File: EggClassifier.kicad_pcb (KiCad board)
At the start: 2 copper layers, 100 x 100 mm, 54 parts, among them J1 Left_02x24, J10 LCD_CHAR, J11 SERVO2, J12 BME280, J13 UART1, J14 FAN, J15 UART2, J16 AS7265X, J17 TFT_SPI, J2 Right Header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

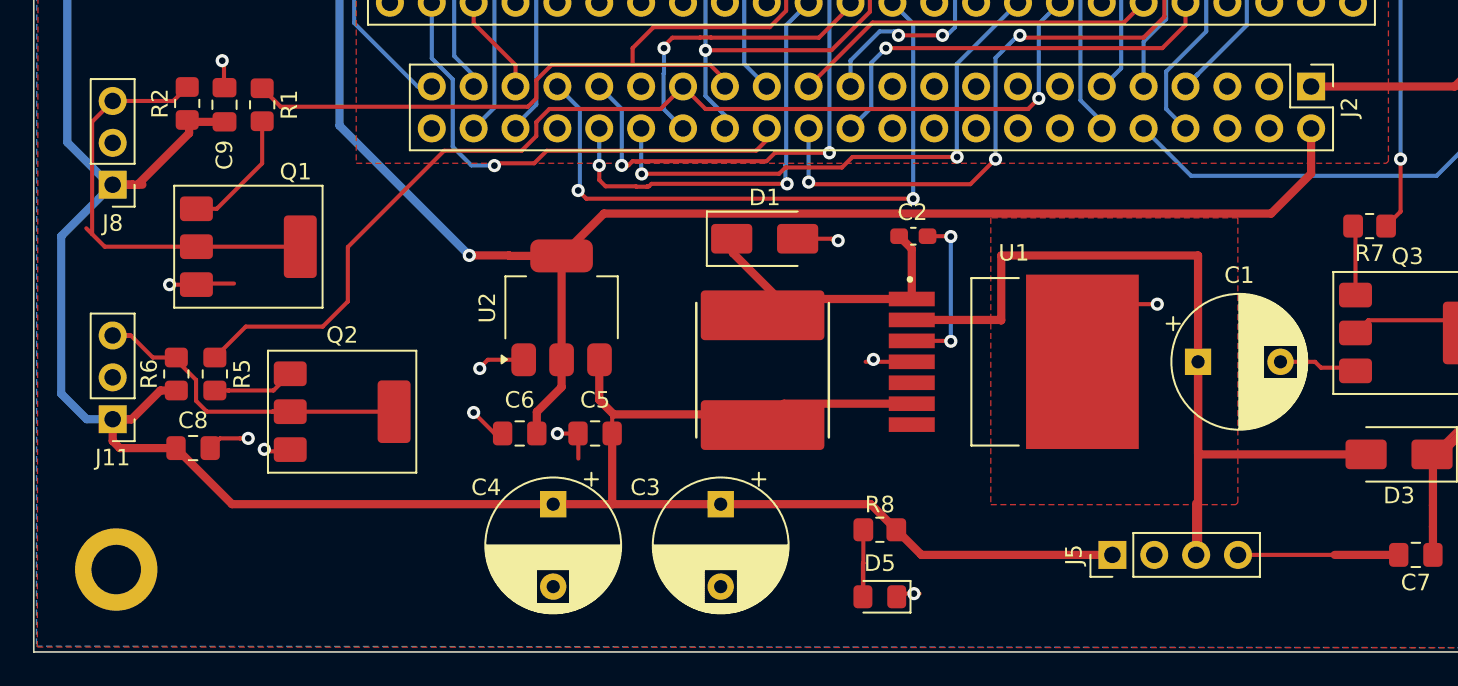
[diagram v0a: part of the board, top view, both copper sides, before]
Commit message: resize electrolytic capacitors hole size to be the same as the connector pins.
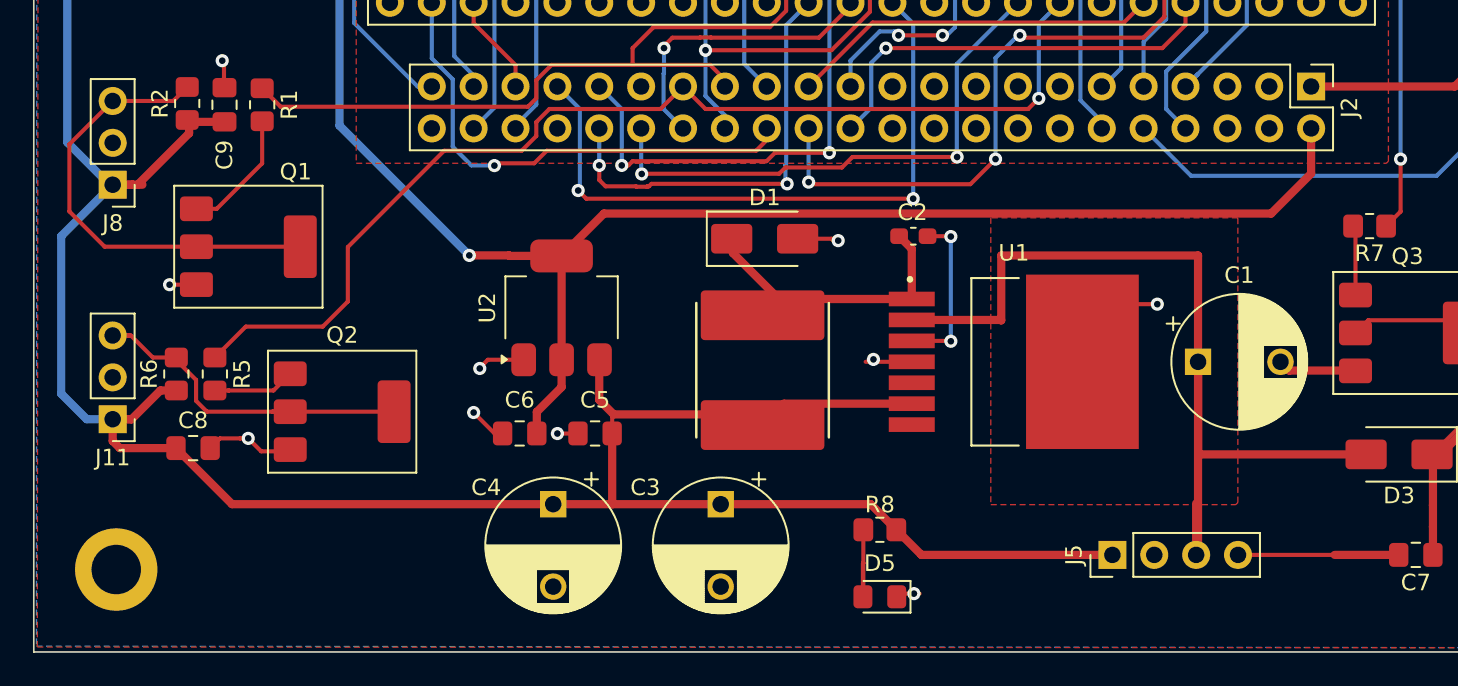
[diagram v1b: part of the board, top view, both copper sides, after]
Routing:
- net GND: track 104.3 -> 102.0 mm, vias 25 -> 24
- net Net-(J8-Pin_3): track 26.9 -> 27.6 mm
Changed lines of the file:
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@@
 		(tags "CP Radial series Radial pin pitch 5.00mm  diameter 8mm Electrolytic Capacitor")
 		(property "Reference" "C4"
-			(at -1.016 4.064 180)
+			(at -1.016 4.064 0)
 			(layer "F.SilkS")
 			(effects
@@
 		)
 		(property "Value" "100uF"
-			(at 7.902 0.508 180)
+			(at 7.902 0.508 0)
 			(layer "F.Fab")
 			(effects
@@
 			(at 0 0 270)
 			(size 1.6 1.6)
-			(drill 0.8)
+			(drill 1)
 			(layers "*.Cu" "*.Mask")
 			(remove_unused_layers no)
@@
 			(at 5 0 270)
 			(size 1.6 1.6)
-			(drill 0.8)
+			(drill 1)
 			(layers "*.Cu" "*.Mask")
 			(remove_unused_layers no)
@@
 		(tags "CP Radial series Radial pin pitch 5.00mm  diameter 8mm Electrolytic Capacitor")
 		(property "Reference" "C3"
-			(at -1.016 4.572 180)
+			(at -1.016 4.572 0)
 			(layer "F.SilkS")
 			(effects
@@
 		)
 		(property "Value" "100uF"
-			(at 7.648 0 180)
+			(at 7.648 0 0)
 			(layer "F.Fab")
 			(effects
@@
 			(at 0 0 270)
 			(size 1.6 1.6)
-			(drill 0.8)
+			(drill 1)
 			(layers "*.Cu" "*.Mask")
 			(remove_unused_layers no)
@@
 			(at 5 0 270)
 			(size 1.6 1.6)
-			(drill 0.8)
+			(drill 1)
 			(layers "*.Cu" "*.Mask")
 			(remove_unused_layers no)
@@
 			(at 0 0)
 			(size 1.6 1.6)
-			(drill 0.8)
+			(drill 1)
 			(layers "*.Cu" "*.Mask")
 			(remove_unused_layers no)
@@
 			(at 5 0)
 			(size 1.6 1.6)
-			(drill 0.8)
+			(drill 1)
 			(layers "*.Cu" "*.Mask")
 			(remove_unused_layers no)
@@
 	)
 	(segment
-		(start 107.061 122.757)
-		(end 107.542 122.276)
-		(width 0.25)
+		(start 155.622 122.4)
+		(end 156.153 122.931)
+		(width 0.5)
 		(layer "F.Cu")
 		(net 1)
 	)
 	(segment
-		(start 158.075 122.757)
-		(end 159.979 122.757)
+		(start 107.061 122.757)
+		(end 107.542 122.276)
 		(width 0.25)
 		(layer "F.Cu")
@@
 	)
 	(segment
-		(start 113.03 128.27)
-		(end 113.03 126.7675)
-		(width 0.25)
-		(layer "F.Cu")
-		(net 1)
-	)
-	(segment
-		(start 157.718 122.4)
-		(end 158.075 122.757)
-		(width 0.25)
-		(layer "F.Cu")
-		(net 1)
-	)
-	(segment
 		(start 88.2359 117.7226)
 		(end 89.8598 117.7226)
@@
 	)
 	(segment
-		(start 93.9806 127.7083)
-		(end 93.9806 127.83)
-		(width 0.25)
-		(layer "F.Cu")
-		(net 1)
-	)
-	(segment
 		(start 128.5116 115.0496)
 		(end 128.397 114.935)
@@
 	)
 	(segment
+		(start 156.153 122.931)
+		(end 160.153 122.931)
+		(width 0.5)
+		(layer "F.Cu")
+		(net 1)
+	)
+	(segment
 		(start 107.178 83.307)
 		(end 100.193 83.307)
@@
 	)
 	(segment
-		(start 155.622 122.4)
-		(end 157.718 122.4)
+		(start 93.7935 127.83)
+		(end 93.0076 127.0441)
 		(width 0.25)
 		(layer "F.Cu")
@@
 	)
 	(segment
-		(start 92.1439 117.652)
-		(end 89.9304 117.652)
-		(width 0.25)
-		(layer "F.Cu")
-		(net 1)
-	)
-	(segment
-		(start 93.9806 127.83)
-		(end 95.4496 127.83)
-		(width 0.25)
-		(layer "F.Cu")
-		(net 1)
-	)
-	(segment
 		(start 158.905 134.112)
 		(end 153.045 134.112)
@@
 		(net 1)
 	)
+	(segment
+		(start 95.4496 127.83)
+		(end 93.7935 127.83)
+		(width 0.25)
+		(layer "F.Cu")
+		(net 1)
+	)
 	(via
 		(at 88.2359 117.7226)
@@
 	)
 	(via
-		(at 93.9806 127.7083)
-		(size 0.8)
-		(drill 0.4)
-		(layers "F.Cu" "B.Cu")
-		(net 1)
-	)
-	(via
 		(at 169.0604 67.7789)
 		(size 0.8)
@@
 	)
 	(segment
-		(start 83.5376 114.6526)
-		(end 83.5376 107.8364)
+		(start 84.2976 115.4176)
+		(end 82.159 113.279)
+		(width 0.25)
+		(layer "F.Cu")
+		(net 132)
+	)
+	(segment
+		(start 82.159 113.279)
+		(end 82.159 109.2046)
 		(width 0.25)
 		(layer "F.Cu")
@@
 	)
 	(segment
-		(start 84.303 115.418)
-		(end 83.185 114.3)
+		(start 89.8648 115.4176)
+		(end 84.2976 115.4176)
 		(width 0.25)
 		(layer "F.Cu")
@@
 	)
 	(segment
-		(start 83.5376 107.8364)
-		(end 84.7852 106.5888)
+		(start 82.159 109.2046)
+		(end 84.7852 106.5784)
 		(width 0.25)
 		(layer "F.Cu")
@@
 	)
 	(segment
-		(start 96.1648 115.418)
-		(end 84.303 115.418)
+		(start 89.8648 115.4176)
+		(end 96.1648 115.4176)
 		(width 0.25)
 		(layer "F.Cu")

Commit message: snapshot
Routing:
- net USER_GPIO4: track 142.7 -> 109.8 mm
- net UART2_RX: track 58.3 -> 59.9 mm
- net +3.3V: track 250.8 -> 251.8 mm, vias 11 -> 12
- net USER_GPIO3: track 83.1 -> 83.9 mm
- net I2C1_SCL: track 71.7 -> 72.4 mm
- net UART1_RX: track 40.3 -> 39.6 mm
- net CAM_HS: track 93.2 -> 93.7 mm
- net TFT_RS: track 79.3 -> 79.2 mm, vias 5 -> 4

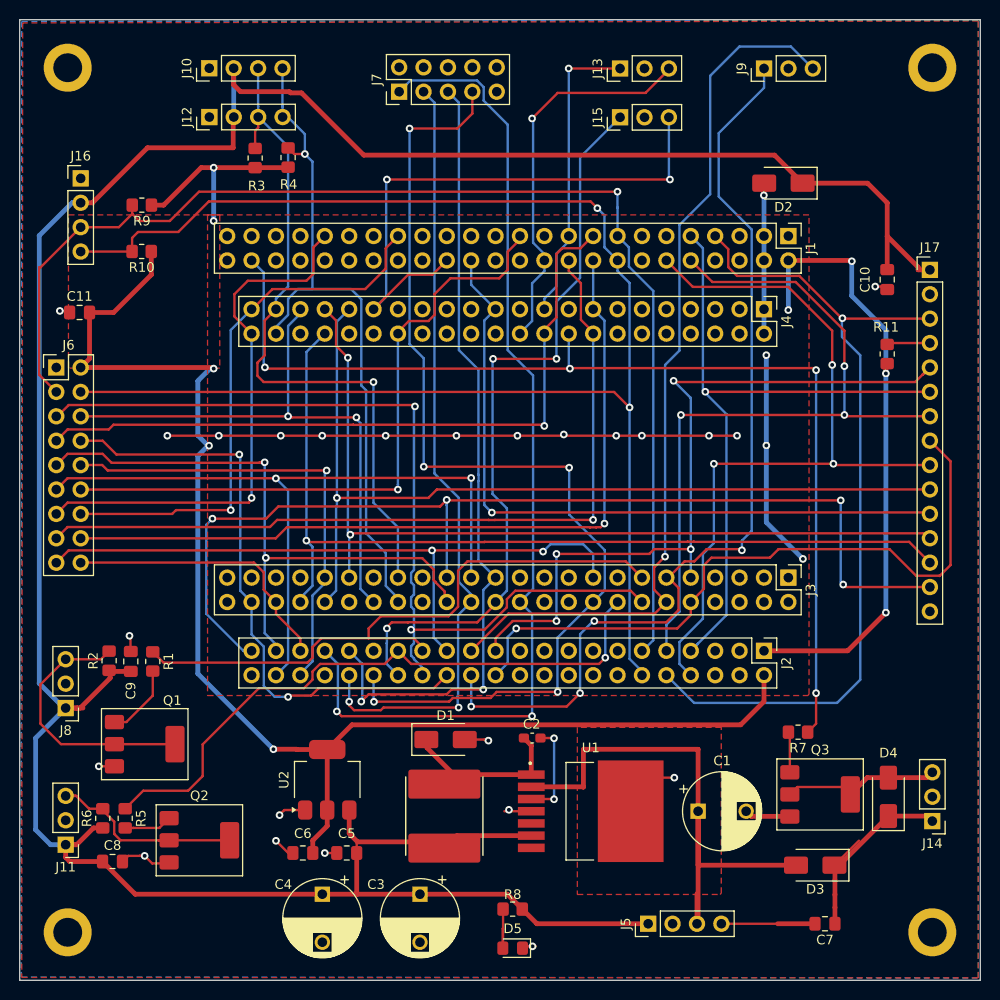
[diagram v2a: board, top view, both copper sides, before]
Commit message: change capacitor footprint
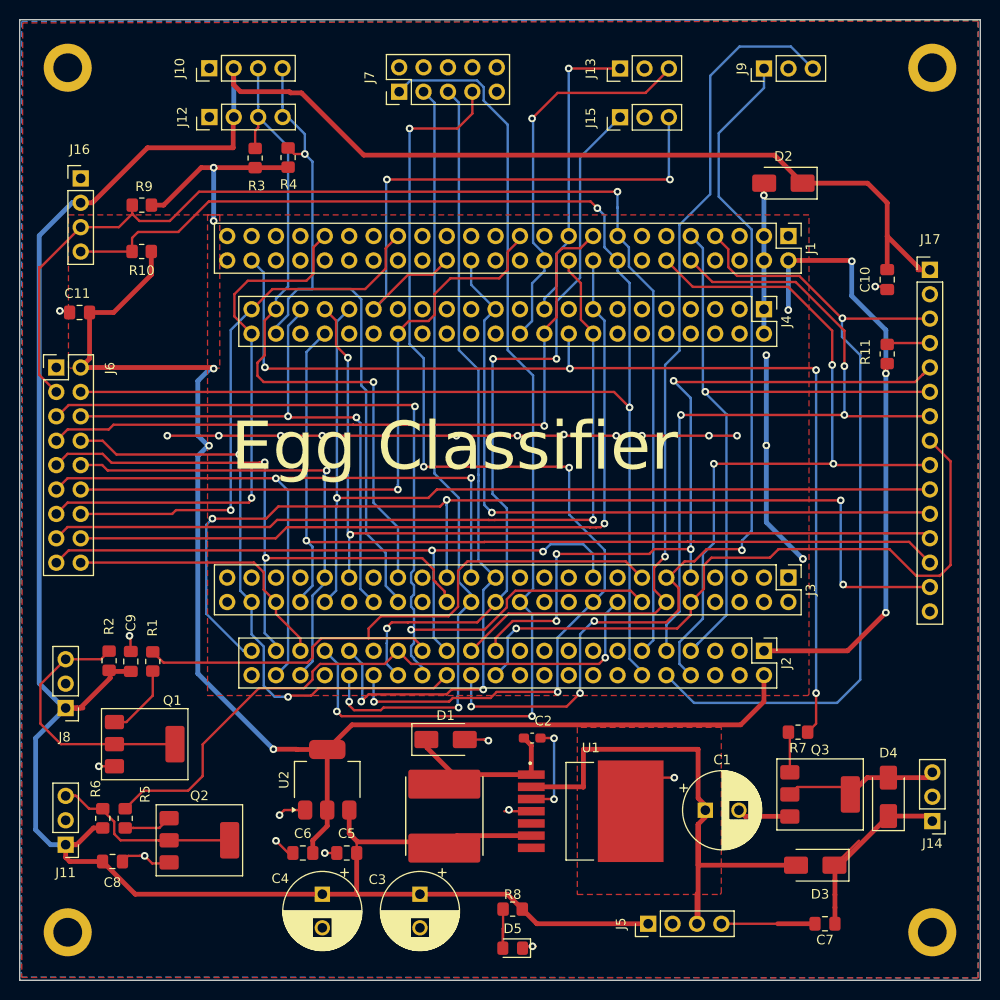
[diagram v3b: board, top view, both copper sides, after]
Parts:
- C1: footprint Capacitor_THT:CP_Radial_D8.0mm_P5.00mm -> EggClassifier:CP_Radial_D8.0mm_P3.50mm
- C3, C4: value 100uF -> 220uF; footprint Capacitor_THT:CP_Radial_D8.0mm_P5.00mm -> EggClassifier:CP_Radial_D8.0mm_P3.50mm
- moved C1 0.76 mm to (151.4, 122.3)
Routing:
- net +12V: track 58.0 -> 56.8 mm
- net GND: track 102.0 -> 102.8 mm
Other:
- board text added: "Egg Classifier"

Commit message: adjust schematic and PCB to reflect as build condition
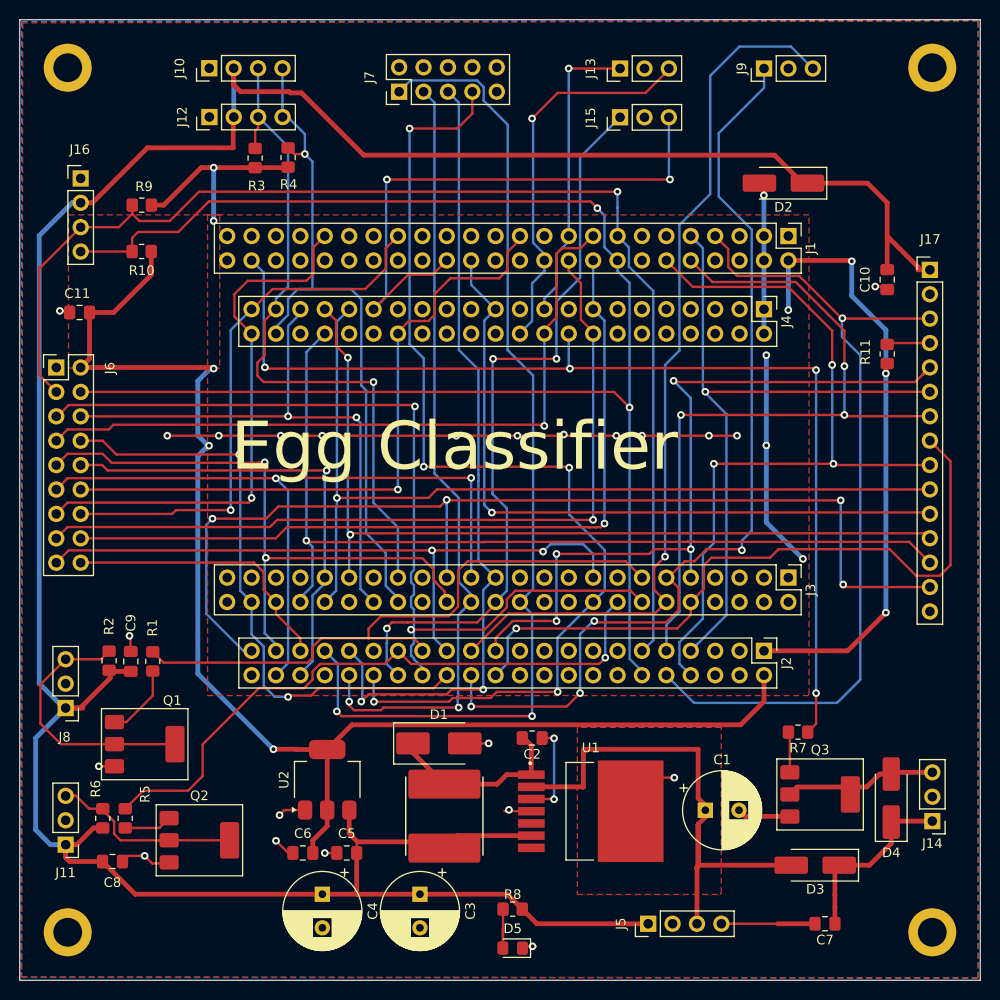
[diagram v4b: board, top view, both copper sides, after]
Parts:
- C1, C3, C4: footprint EggClassifier:CP_Radial_D8.0mm_P3.50mm -> Capacitor_THT:CP_Radial_D8.0mm_P3.50mm
- C2: value 102 -> 103; footprint Capacitor_SMD:C_0603_1608Metric_Pad1.08x0.95mm_HandSolder -> Capacitor_SMD:C_0805_2012Metric_Pad1.18x1.45mm_HandSolder
- D1: value SS36 -> SS56BF; footprint Diode_SMD:D_SMA -> Diode_SMD:D_SMB_Handsoldering
- D2, D3, D4: footprint Diode_SMD:D_SMA -> Diode_SMD:D_SMA_Handsoldering
- R11: value 10K -> 4.7K
- R8: value 330 -> 4.7K
- moved D1 0.80 mm to (123.6, 115.3)
- moved D4 0.32 mm to (170.7, 121.0)
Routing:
- net +12V: track 56.8 -> 54.1 mm
- net Net-(D1-K): track 16.9 -> 19.2 mm
- net Net-(D3-K): track 26.5 -> 24.4 mm
- net Net-(D4-A): track 16.9 -> 15.5 mm

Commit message: moved connectors
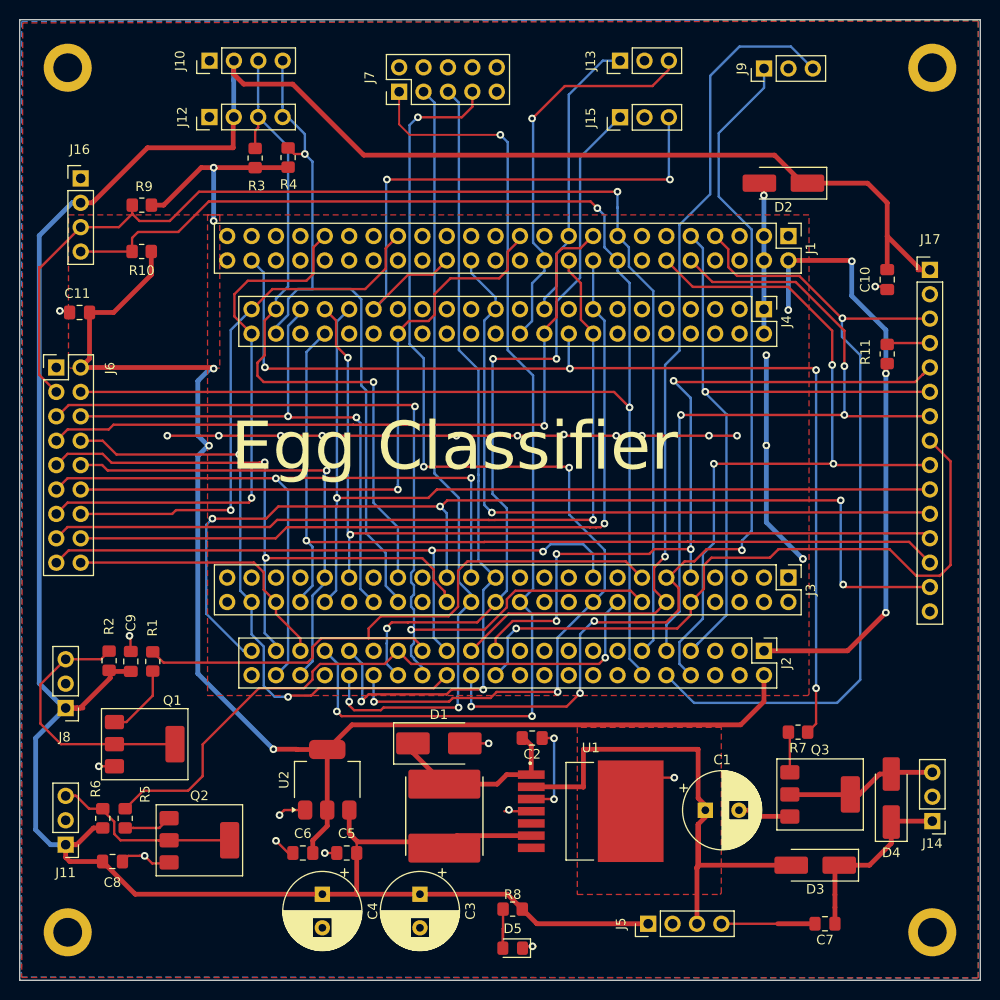
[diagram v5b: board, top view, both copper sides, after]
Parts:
- moved J13 0.81 mm to (142.5, 44.3)
- moved J10 0.79 mm to (99.8, 44.3)
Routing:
- net UART1_TX: track 30.9 -> 29.6 mm, vias 1 -> 0
- net USER_GPIO1: track 105.7 -> 104.8 mm, vias 2 -> 3
- net VCC: track 297.4 -> 298.2 mm
- net I2C1_SDA: track 71.8 -> 72.6 mm
- net I2C1_SCL: track 72.4 -> 73.2 mm
